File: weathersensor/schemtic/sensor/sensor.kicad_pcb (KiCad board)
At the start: 2 copper layers, 1 part, among them U1 ESP32-DEVKITC-32D

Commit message: Start commit message
21.03.2023
	- create and pcb for weathersensor

22.02.2023
	- add schematic and pcb for mqtt_wlan_bridge
	- remove old from git repo

	TODO:
	- create schematic and pcb for weathersensor
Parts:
- added ?: , , F.Cu at (175.1, 18.0)
- added ?: , , F.Cu at (175.1, 87.5)
- added C1: 1.0u, Capacitor_SMD:C_1206_3216Metric, F.Cu at (137.9, 69.2)
- added C10: 220n, Capacitor_SMD:C_1206_3216Metric, F.Cu at (149.0, 62.7)
- added C11: 100n, Capacitor_SMD:C_1206_3216Metric, F.Cu at (95.6, 67.7)
- added C12: 1u, Capacitor_SMD:C_1206_3216Metric, F.Cu at (114.5, 62.1)
- added C13: 100n, Capacitor_SMD:C_1206_3216Metric, F.Cu at (125.4, 21.2)
- added C14: 0.1u, Capacitor_SMD:C_1206_3216Metric, F.Cu at (154.0, 44.8)
- added C15: 0.1u, Capacitor_SMD:C_1206_3216Metric, F.Cu at (164.5, 37.7)
- added C16: 10n, Capacitor_SMD:C_1206_3216Metric, F.Cu at (165.7, 44.8)
- added C2: 1.0u, Capacitor_SMD:C_1206_3216Metric, F.Cu at (137.9, 62.0)
- added C3: 10u, Capacitor_SMD:C_1206_3216Metric, F.Cu at (130.5, 62.0)
- added C4: 47u/16V, Capacitor_SMD:CP_Elec_5x5.3, F.Cu at (155.9, 67.0)
- added C5: 10n, Capacitor_SMD:C_1206_3216Metric, F.Cu at (155.9, 62.8)
- added C6: 100n, Capacitor_SMD:C_1206_3216Metric, F.Cu at (171.1, 62.4)
- added C7: 22n, Capacitor_SMD:C_1206_3216Metric, F.Cu at (174.0, 56.8)
- added C8: 100n, Capacitor_SMD:C_1206_3216Metric, F.Cu at (138.1, 85.4)
- added C9: 47u/16V, Capacitor_SMD:CP_Elec_5x5.3, F.Cu at (144.6, 67.1)
- added D1: BAT60A, Diode_SMD:D_SOD-323, F.Cu at (128.2, 72.2)
- added D2: LED, LED_SMD:LED_1206_3216Metric, F.Cu at (126.6, 66.7)
- added D5: SSB43L, Diode_SMD:D_SMB, F.Cu at (166.8, 69.5)
- added D6: SSB43L, Diode_SMD:D_SMB, F.Cu at (171.7, 69.5)
- added IC1: CN3791, CN3791:SSOP10, F.Cu at (167.9, 58.8)
- added IC2: DW01A, DW01A:SOT23-6, F.Cu at (135.2, 85.4)
- added J1: I2C, Connector_JST:JST_XH_B4B-XH-AM_1x04_P2.50mm_Vertical, F.Cu at (101.5, 20.4)
- added J2: PANEL, TerminalBlock:TerminalBlock_Altech_AK300-2_P5.00mm, F.Cu at (142.1, 77.9)
- added J3: BAT, Connector_JST:JST_XH_B2B-XH-AM_1x02_P2.50mm_Vertical, F.Cu at (125.2, 82.0)
- added J4: ANT, Connector_Coaxial:SMA_Amphenol_901-144_Vertical, F.Cu at (138.2, 20.9)
- added J5: PT1000, Connector_JST:JST_XH_B4B-XH-AM_1x04_P2.50mm_Vertical, F.Cu at (171.7, 49.1)
- added L1: 82u, Inductor_SMD:L_12x12mm_H8mm, F.Cu at (157.2, 77.5)
- added P1: USB_C_Plug_USB2.0, Connector_USB:USB_C_Receptacle_HRO_TYPE-C-31-M-12, F.Cu at (113.0, 83.4)
- added Q1: IRLML6401, Package_TO_SOT_SMD:SOT-23, F.Cu at (132.5, 72.2)
- added Q2: AO3401A, Package_TO_SOT_SMD:SOT-23, F.Cu at (162.6, 63.8)
- added Q3: FS8205, FS8205:SOT95P280X145-6N, F.Cu at (136.5, 76.9)
- added Q4: BSS138, Package_TO_SOT_SMD:SOT-23, F.Cu at (114.1, 65.6)
- added Q5: BSS138, Package_TO_SOT_SMD:SOT-23, F.Cu at (119.2, 65.6)
- added R1: 10k, Resistor_SMD:R_1206_3216Metric, F.Cu at (118.6, 73.2)
- added R10: 1k, Resistor_SMD:R_1206_3216Metric, F.Cu at (136.2, 81.3)
- added R11: 5k1, Resistor_SMD:R_1206_3216Metric, F.Cu at (109.8, 75.7)
- added R12: 10k, Resistor_SMD:R_1206_3216Metric, F.Cu at (122.9, 21.2)
- added R13: 10k, Resistor_SMD:R_1206_3216Metric, F.Cu at (120.5, 21.2)
- added R14: 10k, Resistor_SMD:R_1206_3216Metric, F.Cu at (157.1, 37.7)
- added R15: 10k, Resistor_SMD:R_1206_3216Metric, F.Cu at (159.6, 37.7)
- added R16: 10k, Resistor_SMD:R_1206_3216Metric, F.Cu at (162.0, 37.7)
- added R17: 4k 1% or better, Resistor_SMD:R_1206_3216Metric, F.Cu at (159.0, 49.4)
- added R2: 10k, Resistor_SMD:R_1206_3216Metric, F.Cu at (137.9, 64.5)
- added R3: 1k, Resistor_SMD:R_1206_3216Metric, F.Cu at (129.1, 66.7)
- added R4: 5k1, Resistor_SMD:R_1206_3216Metric, F.Cu at (114.8, 75.7)
- added R5: 120, Resistor_SMD:R_1206_3216Metric, F.Cu at (171.1, 56.8)
- added R6: 22k, Resistor_SMD:R_1206_3216Metric, F.Cu at (157.9, 56.8)
- added R7: 178k, Resistor_SMD:R_1206_3216Metric, F.Cu at (157.9, 59.2)
- added R8: 100, Resistor_SMD:R_1206_3216Metric, F.Cu at (125.8, 76.8)
- added R9: 0.05, Resistor_SMD:R_1206_3216Metric, F.Cu at (149.0, 67.6)
- added REF**: MountingHole_3.2mm_M3, MountingHole:MountingHole_3.2mm_M3, F.Cu at (95.5, 86.0)
- added U2: CH340C, Package_SO:SOIC-16_3.9x9.9mm_P1.27mm, F.Cu at (102.0, 74.5)
- added U3: MS5611-01BA, Package_LGA:LGA-8_3x5mm_P1.25mm, F.Cu at (116.0, 21.1)
- added U4: RFM95W-868S2, RF_Module:HOPERF_RFM9XW_THT, F.Cu at (145.2, 40.7)
- added U5: ESP32-WROOM-32D, RF_Module:ESP32-WROOM-32, F.Cu at (116.7, 42.3)
- added U6: MAX17048G, MAX17048G:SON50P200X200X80-9N, F.Cu at (123.7, 60.4)
- added U7: MAX31865xTP, Package_DFN_QFN:TQFN-20-1EP_5x5mm_P0.65mm_EP3.25x3.25mm, F.Cu at (159.3, 45.0)
- U1: value ESP32-DEVKITC-32D -> XC6220B331MR; footprint ESP32-DEVKITC-32D:MODULE_ESP32-DEVKITC-32D -> Package_TO_SOT_SMD:SOT-23-5
- moved U1 34.8 mm to (133.0, 66.3), turned to 90 degrees
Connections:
- U1 pad 1: unconnected-(U1-Pad1) -> Net-(C1-Pad2)
- U1 pad 2: unconnected-(U1-Pad2) -> GND
- U1 pad 3: unconnected-(U1-Pad3) -> Net-(R2-Pad2)
- U1 pad 5: unconnected-(U1-Pad5) -> +3.3V
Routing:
- net +3.3V: track 0.00 -> 223.9 mm, vias 0 -> 4
- net MOSI: track 0.00 -> 130.6 mm, vias 0 -> 2
- net SCL: track 0.00 -> 79.9 mm, vias 0 -> 3
- net ESP32_RX: track 0.00 -> 76.9 mm
- net ESP32_TX: track 0.00 -> 74.5 mm
- net VSS: track 0.00 -> 73.3 mm
- net V_BAT: track 0.00 -> 60.6 mm, vias 0 -> 2
- net SDA: track 0.00 -> 58.9 mm, vias 0 -> 2
- net SCK: track 0.00 -> 58.5 mm, vias 0 -> 3
- net MISO: track 0.00 -> 57.7 mm, vias 0 -> 5
- net V_USB: track 0.00 -> 47.8 mm
- net RFM_RESET: track 0.00 -> 44.1 mm, vias 0 -> 1
- net Net-(D5-Pad1): track 0.00 -> 43.0 mm
- net Net-(IC1-Pad7): track 0.00 -> 42.4 mm
- net MAX_CS: track 0.00 -> 41.9 mm
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- added copper zone on B.Cu, net GND
- added copper zone on F.Cu, net GND
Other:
- board outline added: 87 x 75 mm

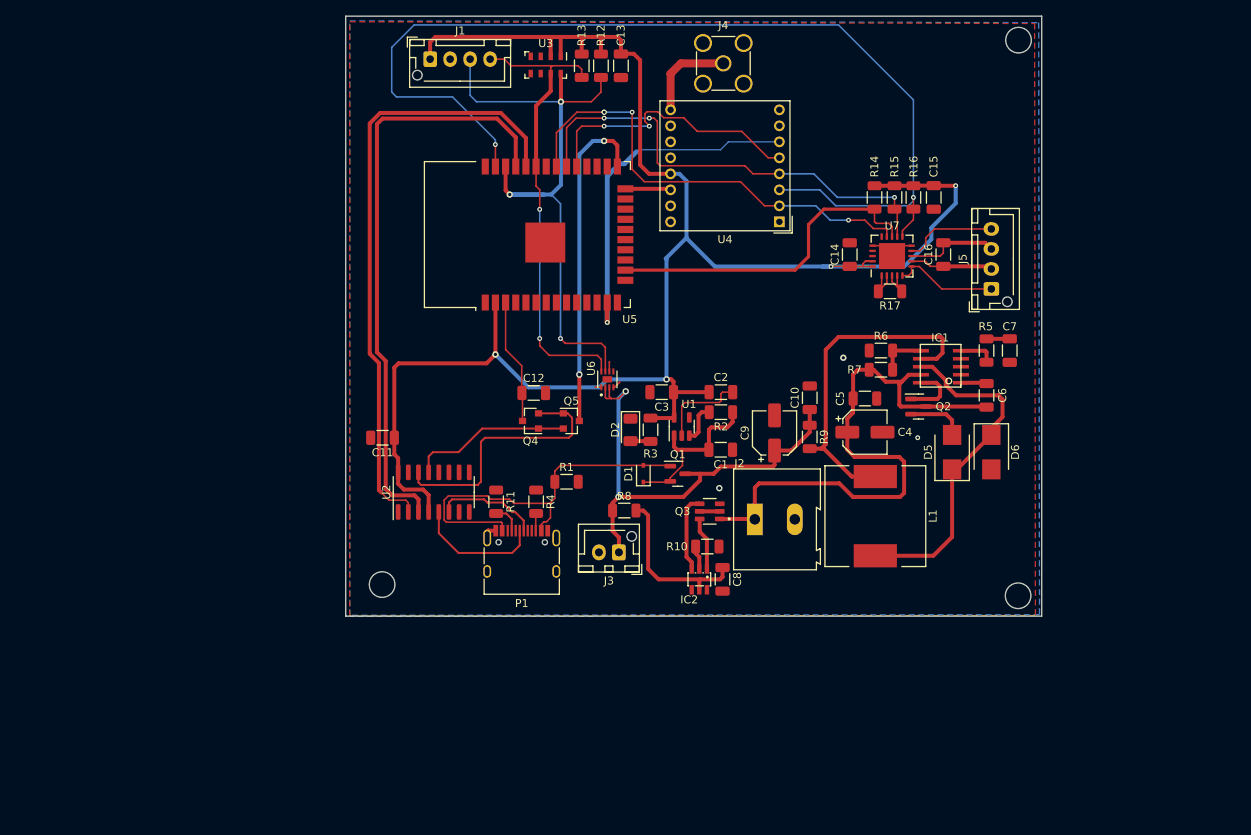
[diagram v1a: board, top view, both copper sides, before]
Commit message: Changes in Source Code:
    use the interal ADC for measure battery and panel voltage
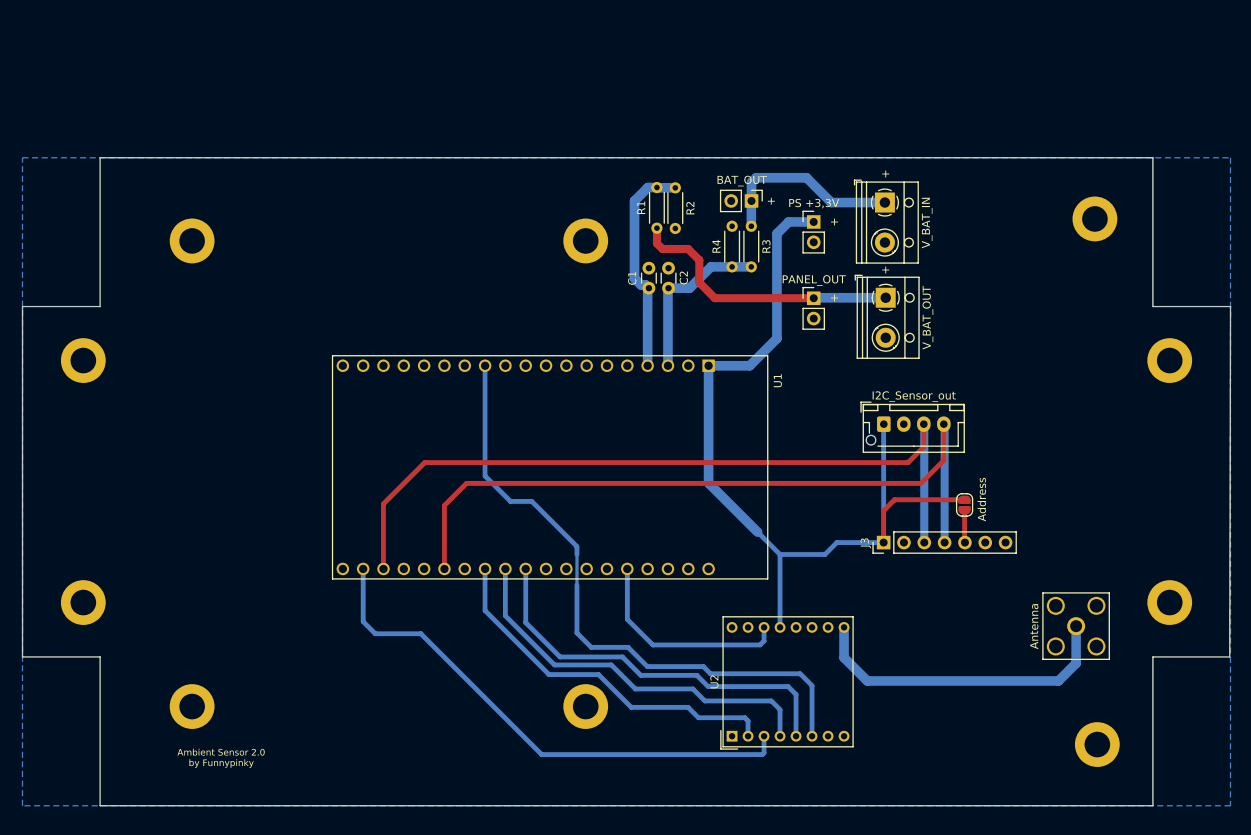
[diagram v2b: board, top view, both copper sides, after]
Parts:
- removed ? (x2): , 
- removed C10: 220n, Capacitor_SMD:C_1206_3216Metric
- removed C11, C13, C6, C8: 100n, Capacitor_SMD:C_1206_3216Metric
- removed C12: 1u, Capacitor_SMD:C_1206_3216Metric
- removed C14, C15: 0.1u, Capacitor_SMD:C_1206_3216Metric
- removed C16, C5: 10n, Capacitor_SMD:C_1206_3216Metric
- removed C3: 10u, Capacitor_SMD:C_1206_3216Metric
- removed C4, C9: 47u/16V, Capacitor_SMD:CP_Elec_5x5.3
- removed C7: 22n, Capacitor_SMD:C_1206_3216Metric
- removed D1: BAT60A, Diode_SMD:D_SOD-323
- removed D2: LED, LED_SMD:LED_1206_3216Metric
- removed D5, D6: SSB43L, Diode_SMD:D_SMB
- removed IC1: CN3791, CN3791:SSOP10
- removed IC2: DW01A, DW01A:SOT23-6
- removed J1: I2C, Connector_JST:JST_XH_B4B-XH-AM_1x04_P2.50mm_Vertical
- removed J2: PANEL, TerminalBlock:TerminalBlock_Altech_AK300-2_P5.00mm
- removed J4: ANT, Connector_Coaxial:SMA_Amphenol_901-144_Vertical
- removed J5: PT1000, Connector_JST:JST_XH_B4B-XH-AM_1x04_P2.50mm_Vertical
- removed L1: 82u, Inductor_SMD:L_12x12mm_H8mm
- removed P1: USB_C_Plug_USB2.0, Connector_USB:USB_C_Receptacle_HRO_TYPE-C-31-M-12
- removed Q1: IRLML6401, Package_TO_SOT_SMD:SOT-23
- removed Q2: AO3401A, Package_TO_SOT_SMD:SOT-23
- removed Q3: FS8205, FS8205:SOT95P280X145-6N
- removed Q4, Q5: BSS138, Package_TO_SOT_SMD:SOT-23
- removed R10: 1k, Resistor_SMD:R_1206_3216Metric
- removed R11: 5k1, Resistor_SMD:R_1206_3216Metric
- removed R12, R13, R14, R15, R16: 10k, Resistor_SMD:R_1206_3216Metric
- removed R17: 4k 1% or better, Resistor_SMD:R_1206_3216Metric
- removed R5: 120, Resistor_SMD:R_1206_3216Metric
- removed R6: 22k, Resistor_SMD:R_1206_3216Metric
- removed R7: 178k, Resistor_SMD:R_1206_3216Metric
- removed R8: 100, Resistor_SMD:R_1206_3216Metric
- removed R9: 0.05, Resistor_SMD:R_1206_3216Metric
- removed the REF** at (95.5, 86.0)
- removed U3: MS5611-01BA, Package_LGA:LGA-8_3x5mm_P1.25mm
- removed U4: RFM95W-868S2, RF_Module:HOPERF_RFM9XW_THT
- removed U5: ESP32-WROOM-32D, RF_Module:ESP32-WROOM-32
- removed U6: MAX17048G, MAX17048G:SON50P200X200X80-9N
- removed U7: MAX31865xTP, Package_DFN_QFN:TQFN-20-1EP_5x5mm_P0.65mm_EP3.25x3.25mm
- added Address: Address Select, Jumper:SolderJumper-2_P1.3mm_Open_RoundedPad1.0x1.5mm, F.Cu at (168.4, 76.1)
- added Antenna: Conn_Coaxial, Connector_Coaxial:SMA_Amphenol_132203-12_Horizontal, F.Cu at (182.3, 91.2)
- added BAT_OUT: V_BAT_OUT, Connector_PinHeader_2.54mm:PinHeader_1x02_P2.54mm_Vertical, F.Cu at (141.7, 38.1)
- added I2C_Sensor_out: I2C_OUT, Connector_JST:JST_XH_B4B-XH-AM_1x04_P2.50mm_Vertical, F.Cu at (158.3, 66.0)
- added PANEL_OUT: V_PANEL_OUT, Connector_PinHeader_2.54mm:PinHeader_1x02_P2.54mm_Vertical, F.Cu at (149.5, 50.3)
- added PS +3,3V: PS, Connector_PinHeader_2.54mm:PinHeader_1x02_P2.54mm_Vertical, F.Cu at (149.5, 40.7)
- added REF**: MountingHole_3.2mm_M3_DIN965_Pad, MountingHole:MountingHole_3.2mm_M3_DIN965_Pad, F.Cu at (184.9, 106.0)
- added REF**: MountingHole_3.2mm_M3_DIN965_Pad, MountingHole:MountingHole_3.2mm_M3_DIN965_Pad, F.Cu at (184.7, 40.4)
- added REF**: MountingHole_3.2mm_M3_DIN965_Pad, MountingHole:MountingHole_3.2mm_M3_DIN965_Pad, F.Cu at (58.2, 88.3)
- added REF**: MountingHole_3.2mm_M3_DIN965_Pad, MountingHole:MountingHole_3.2mm_M3_DIN965_Pad, F.Cu at (194.0, 88.3)
- added REF**: MountingHole_3.2mm_M3_DIN965_Pad, MountingHole:MountingHole_3.2mm_M3_DIN965_Pad, F.Cu at (58.2, 58.0)
- added REF**: MountingHole_3.2mm_M3_DIN965_Pad, MountingHole:MountingHole_3.2mm_M3_DIN965_Pad, F.Cu at (71.8, 101.3)
- added REF**: MountingHole_3.2mm_M3_DIN965_Pad, MountingHole:MountingHole_3.2mm_M3_DIN965_Pad, F.Cu at (121.0, 43.1)
- added REF**: MountingHole_3.2mm_M3_DIN965_Pad, MountingHole:MountingHole_3.2mm_M3_DIN965_Pad, F.Cu at (71.8, 43.1)
- added REF**: MountingHole_3.2mm_M3_DIN965_Pad, MountingHole:MountingHole_3.2mm_M3_DIN965_Pad, F.Cu at (121.0, 101.3)
- added REF**: MountingHole_3.2mm_M3_DIN965_Pad, MountingHole:MountingHole_3.2mm_M3_DIN965_Pad, F.Cu at (194.0, 58.0)
- added V_BAT_IN: V_BAT_IN, TerminalBlock_RND:TerminalBlock_RND_205-00012_1x02_P5.00mm_Horizontal, F.Cu at (158.4, 38.3)
- added V_BAT_OUT: V_PANEL_IN, TerminalBlock_RND:TerminalBlock_RND_205-00012_1x02_P5.00mm_Horizontal, F.Cu at (158.5, 50.2)
- C1, C2: value 1.0u -> 100nF; footprint Capacitor_SMD:C_1206_3216Metric -> Capacitor_THT:C_Disc_D3.0mm_W1.6mm_P2.50mm
- J3: value BAT -> MS5611; footprint Connector_JST:JST_XH_B2B-XH-AM_1x02_P2.50mm_Vertical -> Connector_PinHeader_2.54mm:PinHeader_1x07_P2.54mm_Vertical
- R1: value 10k -> 10M; footprint Resistor_SMD:R_1206_3216Metric -> Resistor_THT:R_Axial_DIN0204_L3.6mm_D1.6mm_P5.08mm_Horizontal
- R2: value 10k -> 510k; footprint Resistor_SMD:R_1206_3216Metric -> Resistor_THT:R_Axial_DIN0204_L3.6mm_D1.6mm_P5.08mm_Horizontal
- R3: value 1k -> 2.2M; footprint Resistor_SMD:R_1206_3216Metric -> Resistor_THT:R_Axial_DIN0204_L3.6mm_D1.6mm_P5.08mm_Horizontal
- R4: value 5k1 -> 510k; footprint Resistor_SMD:R_1206_3216Metric -> Resistor_THT:R_Axial_DIN0204_L3.6mm_D1.6mm_P5.08mm_Horizontal
- U1: value XC6220B331MR -> ESP32-DevKitC; footprint Package_TO_SOT_SMD:SOT-23-5 -> ESP32-DEVKITC-32D:MODULE_ESP32-DEVKITC-32D
- U2: value CH340C -> RFM95W-868S2; footprint Package_SO:SOIC-16_3.9x9.9mm_P1.27mm -> RF_Module:HOPERF_RFM9XW_THT
- moved U2 48.2 mm to (139.3, 105.0)
- moved R4 38.2 mm to (139.3, 46.3), turned to 90 degrees
- moved R1 33.7 mm to (129.9, 41.5), turned to 90 degrees
- moved J3 33.1 mm to (158.2, 80.8), turned to 90 degrees
- moved R2 28.6 mm to (132.2, 36.5), turned to -90 degrees
- moved R3 28.4 mm to (141.7, 41.3)
- moved C1 22.1 mm to (128.9, 49.0), turned to 90 degrees
- moved U1 17.2 mm to (116.6, 71.4), turned to -90 degrees
- moved C2 14.6 mm to (131.3, 49.0), turned to 90 degrees
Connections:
- C1 pad 1: GND -> V_PANEL
- C1 pad 2: Net-(C1-Pad2) -> GND
- C2 pad 1: +3.3V -> V_BAT
- J3 pad 1: V_BAT -> VCC
- R1 pad 1: V_USB -> Net-(J4-Pad1)
- R1 pad 2: GND -> V_PANEL
- R2 pad 1: Net-(C1-Pad2) -> V_PANEL
- R2 pad 2: Net-(R2-Pad2) -> GND
- R3 pad 1: +3.3V -> Net-(J6-Pad1)
- R3 pad 2: Net-(D2-Pad2) -> V_BAT
- R4 pad 1: GND -> V_BAT
- R4 pad 2: Net-(P1-PadB5) -> GND
- U1 pad 1: Net-(C1-Pad2) -> VCC
- U1 pad 2: GND -> unconnected-(U1-Pad2)
- U1 pad 3: Net-(R2-Pad2) -> V_BAT
- U1 pad 4: unconnected-(U1-Pad4) -> V_PANEL
- U1 pad 5: +3.3V -> unconnected-(U1-Pad5)
- U2 pad 10: unconnected-(U2-Pad10) -> GND
- U2 pad 13: Net-(Q4-Pad1) -> VCC
- U2 pad 14: Net-(Q4-Pad2) -> DI0
- U2 pad 16: +3.3V -> unconnected-(U2-Pad16)
- U2 pad 2: ESP32_RX -> MISO
- U2 pad 3: ESP32_TX -> MOSI
- U2 pad 4: +3.3V -> CLK
- U2 pad 5: Net-(P1-PadA6) -> NSS
- U2 pad 6: Net-(P1-PadA7) -> Net-(U1-Pad12)
- U2 pad 8: unconnected-(U2-Pad8) -> GND
- U2 pad 9: unconnected-(U2-Pad9) -> Net-(J1-Pad1)
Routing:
- net +3.3V: track 223.9 -> 0.00 mm, vias 4 -> 0
- net VCC: track 0.00 -> 107.7 mm
- net Net-(U1-Pad12): track 0.00 -> 78.2 mm
- net ESP32_RX: track 76.9 -> 0.00 mm
- net ESP32_TX: track 74.5 -> 0.00 mm
- net VSS: track 73.3 -> 0.00 mm
- net MOSI: track 130.6 -> 65.8 mm, vias 2 -> 0
- net SCK: track 58.5 -> 0.00 mm, vias 3 -> 0
- net NSS: track 0.00 -> 49.4 mm
- net CLK: track 0.00 -> 48.4 mm
- net V_USB: track 47.8 -> 0.00 mm
- net RFM_RESET: track 44.1 -> 0.00 mm, vias 1 -> 0
- net Net-(D5-Pad1): track 43.0 -> 0.00 mm
- net Net-(IC1-Pad7): track 42.4 -> 0.00 mm
- net MAX_CS: track 41.9 -> 0.00 mm
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- removed copper zone on F.Cu, net GND
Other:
- board size 87 x 75 mm -> 151 x 81 mm
- board text added: "+"
- board text added: "Ambient Sensor 2.0 by Funnypinky"

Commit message: Change to lorawan
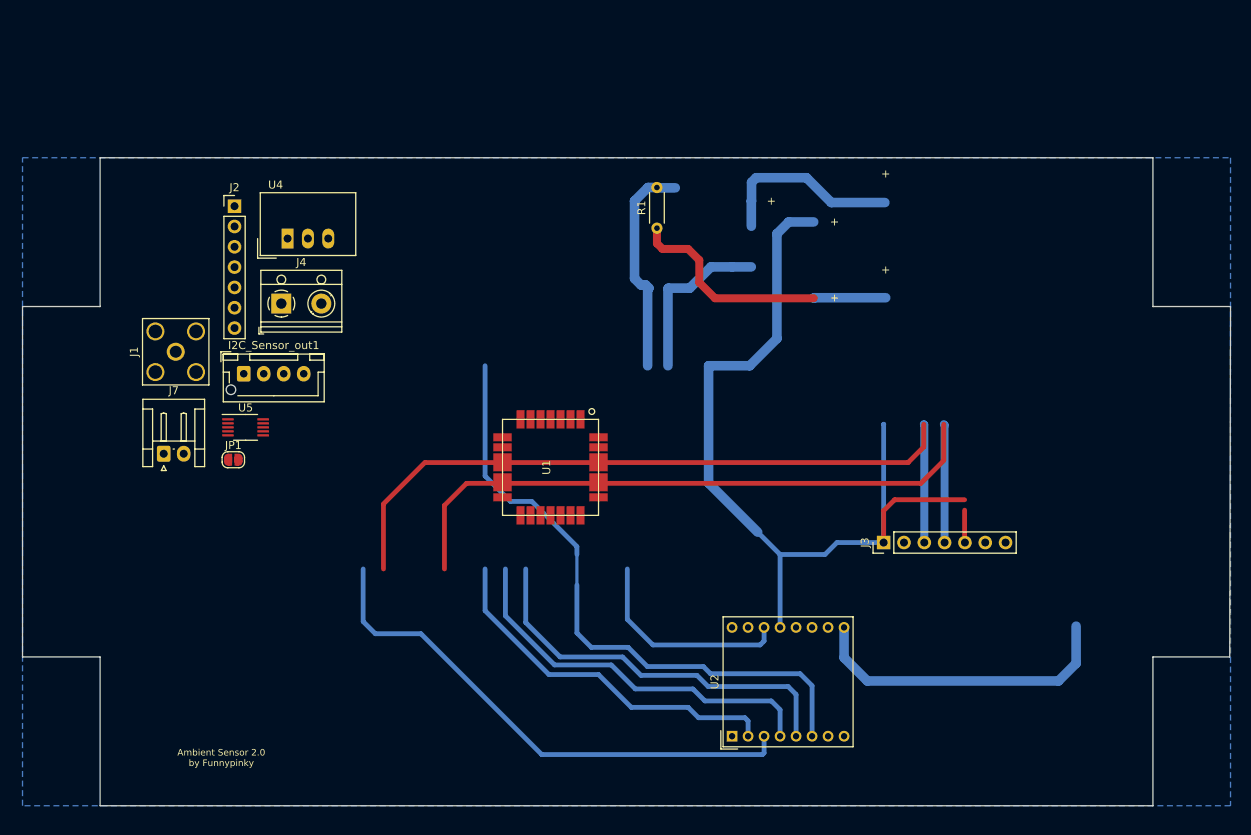
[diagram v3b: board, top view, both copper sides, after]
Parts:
- removed Address: Address Select, Jumper:SolderJumper-2_P1.3mm_Open_RoundedPad1.0x1.5mm
- removed Antenna: Conn_Coaxial, Connector_Coaxial:SMA_Amphenol_132203-12_Horizontal
- removed BAT_OUT: V_BAT_OUT, Connector_PinHeader_2.54mm:PinHeader_1x02_P2.54mm_Vertical
- removed C1, C2: 100nF, Capacitor_THT:C_Disc_D3.0mm_W1.6mm_P2.50mm
- removed I2C_Sensor_out: I2C_OUT, Connector_JST:JST_XH_B4B-XH-AM_1x04_P2.50mm_Vertical
- removed PANEL_OUT: V_PANEL_OUT, Connector_PinHeader_2.54mm:PinHeader_1x02_P2.54mm_Vertical
- removed PS +3,3V: PS, Connector_PinHeader_2.54mm:PinHeader_1x02_P2.54mm_Vertical
- removed R2, R4: 510k, Resistor_THT:R_Axial_DIN0204_L3.6mm_D1.6mm_P5.08mm_Horizontal
- removed R3: 2.2M, Resistor_THT:R_Axial_DIN0204_L3.6mm_D1.6mm_P5.08mm_Horizontal
- removed REF** (x10): MountingHole_3.2mm_M3_DIN965_Pad, MountingHole:MountingHole_3.2mm_M3_DIN965_Pad
- removed V_BAT_IN: V_BAT_IN, TerminalBlock_RND:TerminalBlock_RND_205-00012_1x02_P5.00mm_Horizontal
- removed V_BAT_OUT: V_PANEL_IN, TerminalBlock_RND:TerminalBlock_RND_205-00012_1x02_P5.00mm_Horizontal
- added I2C_Sensor_out1: I2C_OUT, Connector_JST:JST_XH_B4B-XH-AM_1x04_P2.50mm_Vertical, F.Cu at (78.2, 59.7)
- added J1: Conn_Coaxial, Connector_Coaxial:SMA_Amphenol_132203-12_Horizontal, F.Cu at (69.8, 57.0)
- added J2: MS5611, Connector_PinHeader_2.54mm:PinHeader_1x07_P2.54mm_Vertical, F.Cu at (77.1, 38.8)
- added J4: PANEL, TerminalBlock_RND:TerminalBlock_RND_205-00012_1x02_P5.00mm_Horizontal, F.Cu at (83.0, 50.9)
- added J7: BAT, Connector_JST:JST_EH_S2B-EH_1x02_P2.50mm_Horizontal, F.Cu at (68.2, 69.7)
- added JP1: Address Select, Jumper:SolderJumper-2_P1.3mm_Open_RoundedPad1.0x1.5mm, F.Cu at (77.0, 70.5)
- added U4: TSR_1-2450, Converter_DCDC:Converter_DCDC_TRACO_TSR-1_THT, F.Cu at (83.7, 42.8)
- added U5: INA226, Package_SO:VSSOP-10_3x3mm_P0.5mm, F.Cu at (78.5, 66.4)
- U1: value ESP32-DevKitC -> LoRa-E5; footprint ESP32-DEVKITC-32D:MODULE_ESP32-DEVKITC-32D -> LoRa-E5:LoRa-E5
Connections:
- U1 pad 12: Net-(U1-Pad12) -> unconnected-(U1-PC1-Pad12)
- U1 pad 15: unconnected-(U1-Pad15) -> RFIO
- U1 pad 16: unconnected-(U1-Pad16) -> GND
- U1 pad 17: unconnected-(U1-Pad17) -> RST
- U1 pad 2: unconnected-(U1-Pad2) -> GND
- U1 pad 22: unconnected-(U1-Pad22) -> GND
- U1 pad 24: DI0 -> unconnected-(U1-PB13~{}-Pad24)
- U1 pad 3: V_BAT -> SWDIO
- U1 pad 4: V_PANEL -> SWCLK
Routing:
- net Net-(J6-Pad1): track 23.7 -> 0.00 mm
- net (no net): track 0.00 -> 23.7 mm
